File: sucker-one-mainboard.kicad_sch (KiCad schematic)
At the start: 113 parts, among them J1 JST NC Valve, J10 BM10B-SRSS-TB(LF)(SN), J11 UART/SWD DNP, J12 TYPE-C-31-M-12, J2 JST NO Valve, J3 6P4C, J4 JST 3 Way Valve, J5 Jack-DC, J6 Phoenix Contact 1733570, J7 QWIIC I2C, J8 SPI, J9 BM04B-SRSS-TBT(LF)(SN), Q1 BSS138, Q2 BSS138, Q3 BSS138, Q4 STN4NF20L, SW1 BOOTSEL, U1 LD1117S33TR, U2 TPS62143RGTT, U3 W25Q128JVS, U4 RP2040, Y1 ABMM2-12.000MHZ-E2-T

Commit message: WiP Layout Ref 2
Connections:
- net FOOTPEDAL: no longer D1.2 (K)
- net FOOTPEDAL_AUX: no longer D1.1 (K)
- net FPTVS: now reaches J3.2, R24.1
- net FPTVS: now also D1.2 (K)
- net FPATVS: now reaches J3.3, R23.1
- net FPATVS: now also D1.1 (K)
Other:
- moved on the sheet: R23, R24, TP20, TP31

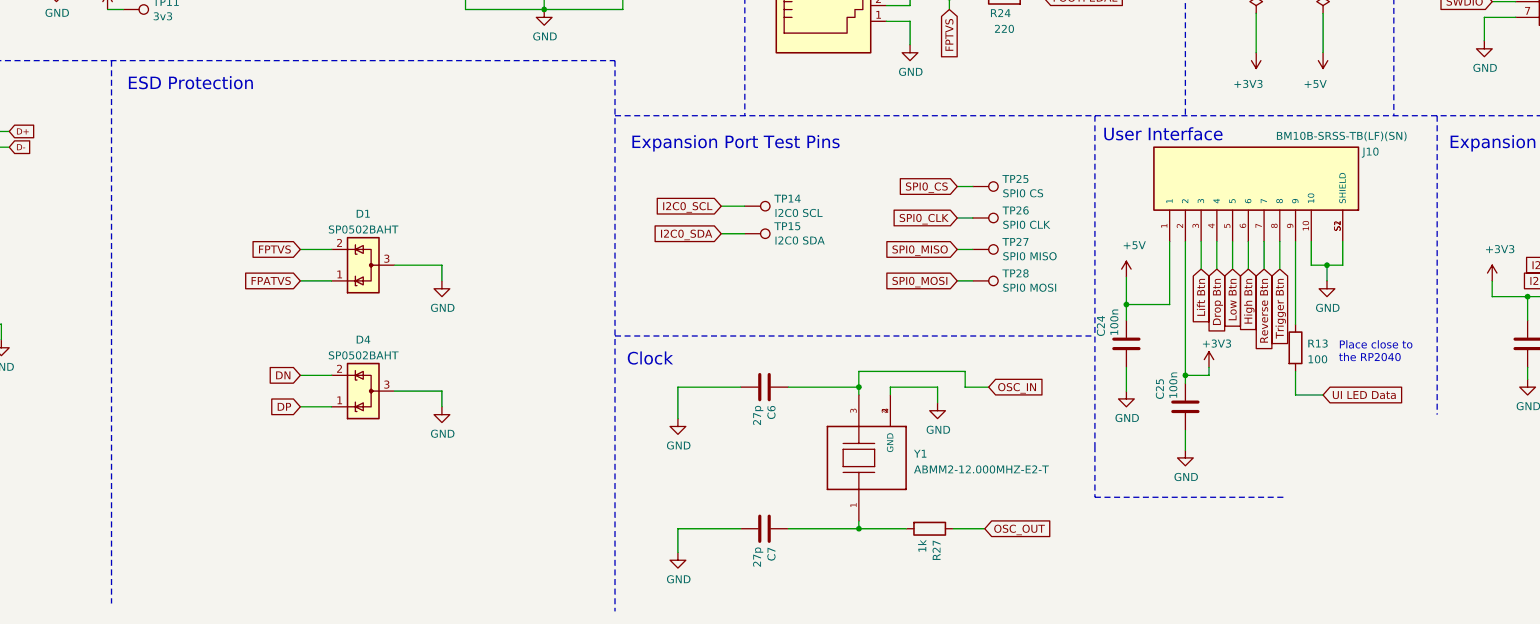
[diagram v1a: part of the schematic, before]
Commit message: Add UI board level shifting
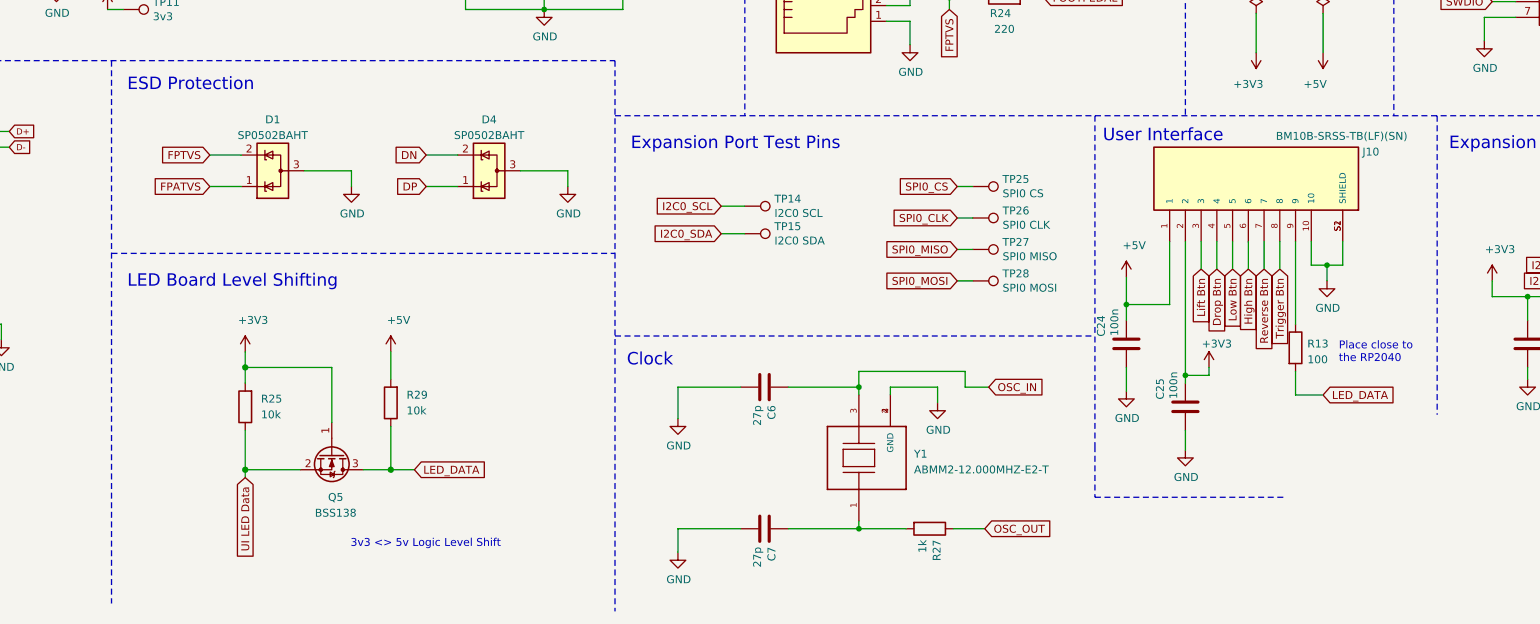
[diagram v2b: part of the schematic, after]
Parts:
- added Q5: BSS138, Package_TO_SOT_SMD:SOT-23, symbol Transistor_FET:BSS138
- added R25, R29: 10k, Resistor_SMD:R_0603_1608Metric, symbol Device:R
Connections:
- net +3V3: now also Q5.1 (G), R25.2
- net +5V: now also R29.2
- net UI LED Data: now also Q5.2 (S), R25.1; no longer R13.2
- new net LED_DATA: Q5.3 (D), R13.2, R29.1
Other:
- note added: "3v3 <> 5v Logic Level Shift"
- note added: "LED Board Level Shifting"
- moved on the sheet: D1, D4

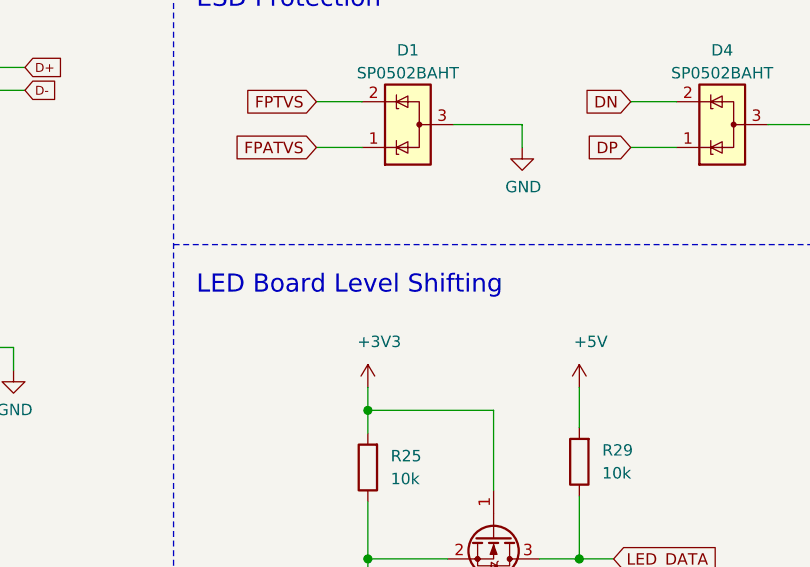
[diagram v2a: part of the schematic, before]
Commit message: Updated pad below RP2040
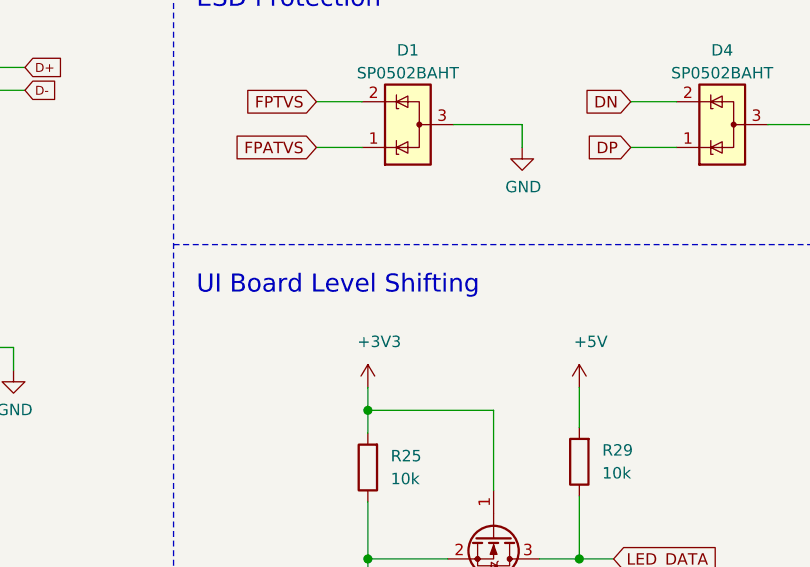
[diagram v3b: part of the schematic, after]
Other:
- note added: "UI Board Level Shifting"
- note removed: "LED Board Level Shifting"
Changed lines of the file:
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@@
     (effects (font (size 2.0066 2.0066)) (justify left bottom))
   )
-  (text "LED Board Level Shifting\n" (at 113.03 232.41 0)
+  (text "UI Board Level Shifting\n" (at 113.03 232.41 0)
     (effects (font (size 2.0066 2.0066)) (justify left bottom))
   )

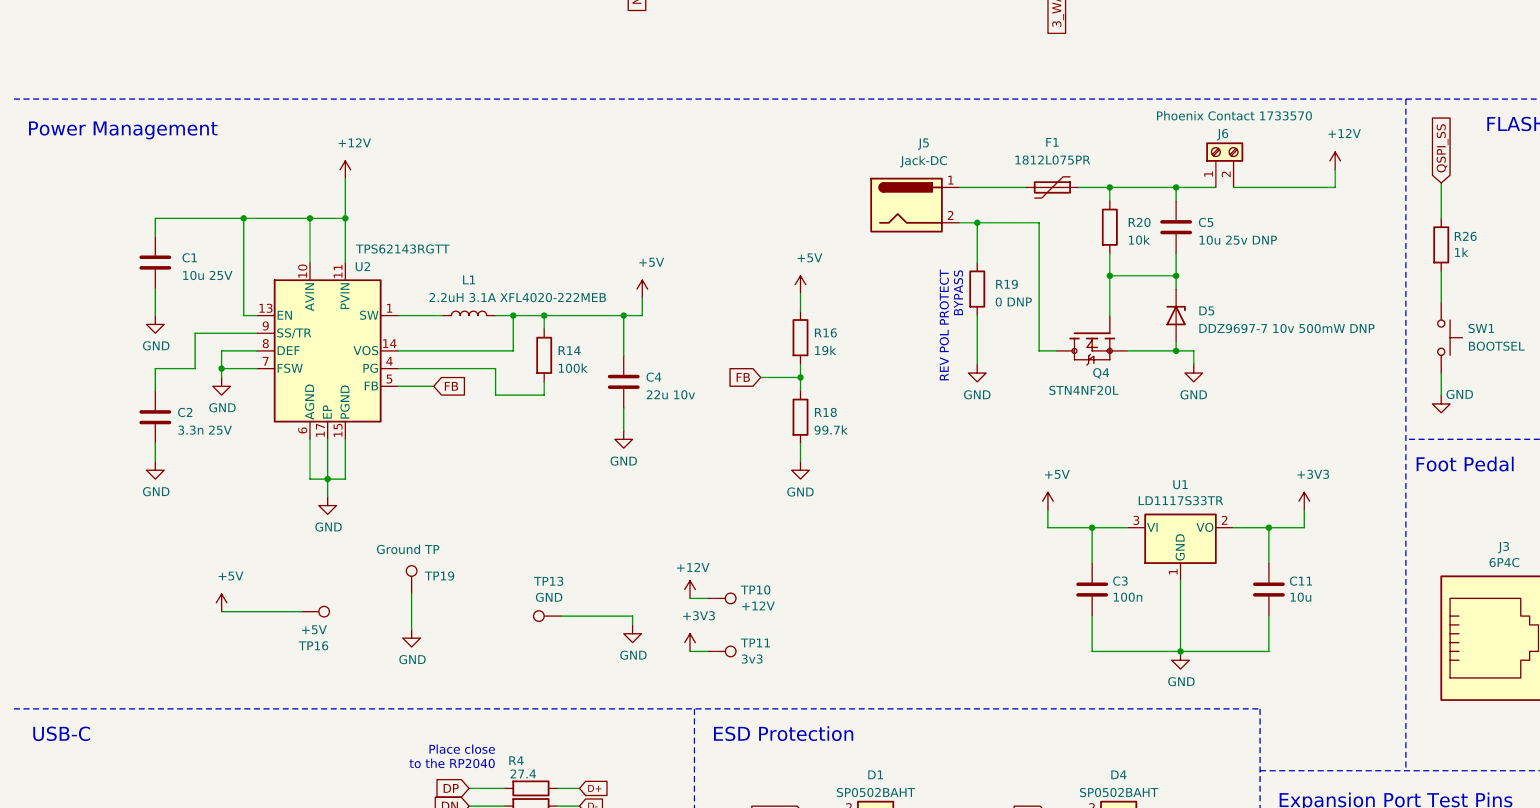
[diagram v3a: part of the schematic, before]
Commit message: Changed Buck Converter
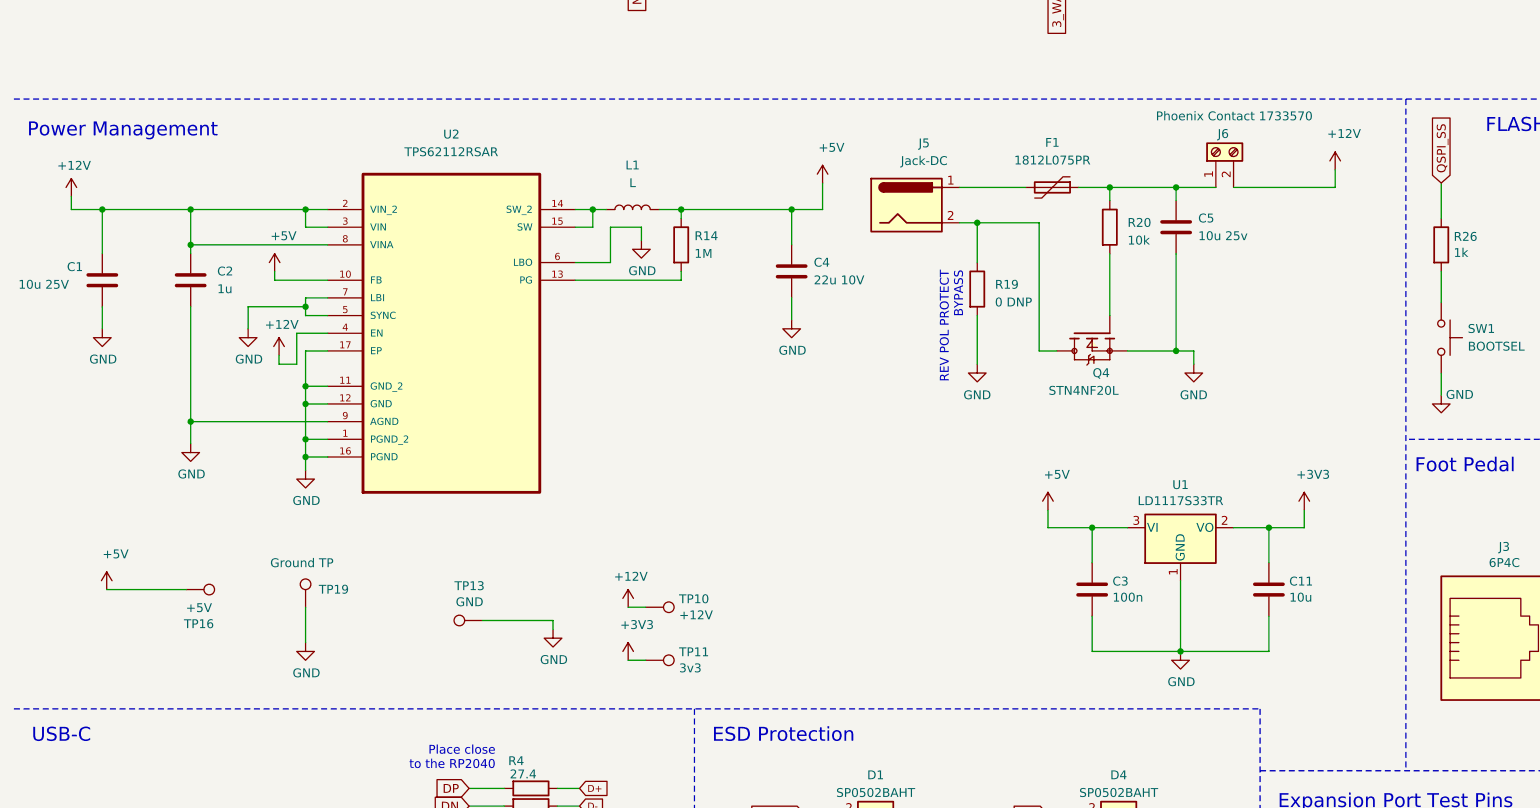
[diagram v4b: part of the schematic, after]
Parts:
- removed D5: DDZ9697-7 10v 500mW DNP, Diode_SMD:D_SOD-123, symbol Device:D_Zener
- removed R16: 19k, Resistor_SMD:R_0603_1608Metric, symbol Device:R
- removed R18: 99.7k, Resistor_SMD:R_0603_1608Metric, symbol Device:R
- removed U2: TPS62143RGTT, Package_DFN_QFN:VQFN-16-1EP_3x3mm_P0.5mm_EP1.68x1.68mm_ThermalVias, symbol Regulator_Switching:TPS62143
- added U2: TPS62112RSAR, TPS62112RSAR:QFN65P400X400X100-17N, symbol TPS62112RSAR:TPS62112RSAR
- C1: Part Number (none) -> C3225X5R1E106K
- C2: value 3.3n 25V -> 1u; footprint Capacitor_SMD:C_0603_1608Metric -> Capacitor_SMD:C_0805_2012Metric
- C4: value 22u 10v -> 22u 10V; footprint Capacitor_SMD:C_0805_2012Metric -> Capacitor_SMD:C_1210_3225Metric
- C5: value 10u 25v DNP -> 10u 25v; footprint Capacitor_SMD:C_0603_1608Metric -> Capacitor_SMD:C_1210_3225Metric; Part (none) -> C3225X5R1E106K
- L1: value 2.2uH 3.1A XFL4020-222MEB -> L; footprint Inductor_SMD:L_Coilcraft_XxL4020 -> Inductor_SMD:L_TDK_SLF7032
- R14: value 100k -> 1M
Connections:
- net +12V: now also C2.1, U2.2 (VIN_2), U2.3 (VIN), U2.4 (EN), U2.8 (VINA)
- net +5V: now also U2.10 (FB)
- net GND: now also C5.2, U2.1 (PGND_2), U2.11 (GND_2), U2.12 (GND), U2.16 (PGND), U2.17 (EP), U2.5 (SYNC), U2.6 (LBO), U2.7 (LBI), U2.9 (AGND)
- net at L1.1: now also U2.14 (SW_2), U2.15 (SW)
- net at R14.2: now also U2.13 (PG)
- net at Q4.1, R20.2: no longer C5.2
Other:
- moved on the sheet: TP10, TP11, TP13, TP16, TP19
